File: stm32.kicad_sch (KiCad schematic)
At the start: 12 parts, among them U1 STM32H743VGTx, Y1 32.768MHz, Y2 LFXTAL078719Cutt

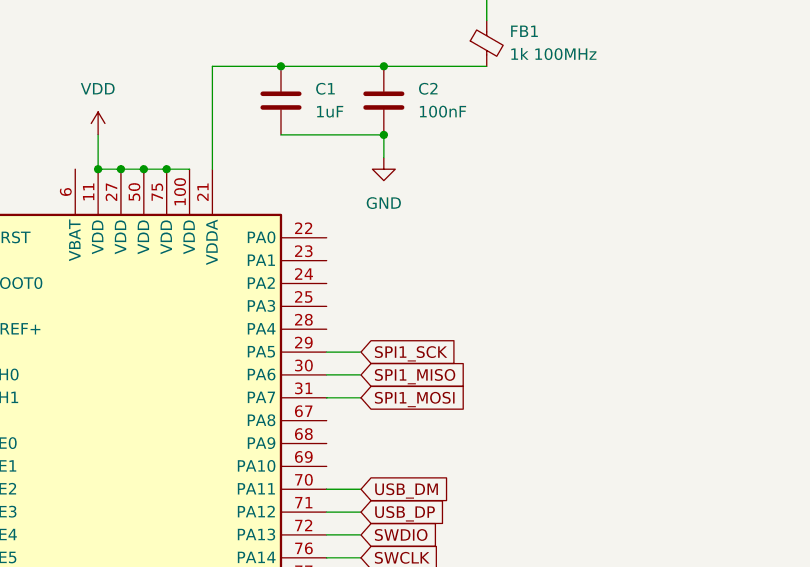
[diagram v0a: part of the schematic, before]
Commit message: Added all sensors and telemetry modem
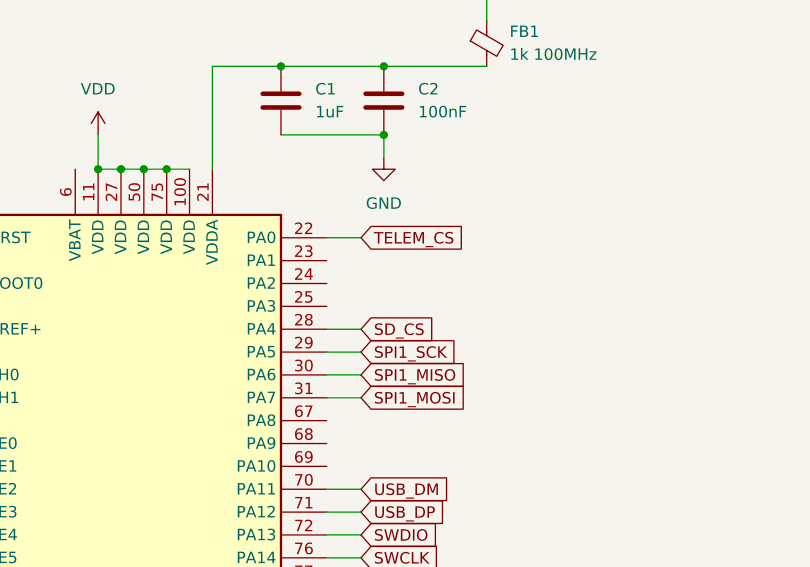
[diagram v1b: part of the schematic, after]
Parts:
- C16, C17, C18, C19: footprint Capacitor_SMD:C_0201_0603Metric -> Capacitor_SMD:C_0402_1005Metric
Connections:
- net TELEM_CS: now reaches U1.22 (PA0)
- net SD_CS: now reaches U1.28 (PA4)
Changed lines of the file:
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@@
+	(wire
+		(pts
+			(xy 152.4 59.69) (xy 156.21 59.69)
+		)
+		(stroke
+			(width 0)
+			(type default)
+		)
+	)
 	(wire
 		(pts
@@
 		(pts
 			(xy 99.06 161.29) (xy 99.06 158.75)
+		)
+		(stroke
+			(width 0)
+			(type default)
+		)
+	)
+	(wire
+		(pts
+			(xy 152.4 49.53) (xy 156.21 49.53)
 		)
 		(stroke
@@
 		(property "Intersheetrefs" "${INTERSHEET_REFS}"
 			(at 166.5128 80.01 0)
+			(effects
+				(font
+					(size 1.27 1.27)
+				)
+				(justify left)
+				(hide yes)
+			)
+		)
+	)
+	(global_label "SD_CS"
+		(shape input)
+		(at 156.21 59.69 0)
+		(fields_autoplaced yes)
+		(effects
+			(font
+				(size 1.27 1.27)
+			)
+			(justify left)
+		)
+		(property "Intersheetrefs" "${INTERSHEET_REFS}"
+			(at 165.1218 59.69 0)
+			(effects
+				(font
+					(size 1.27 1.27)
+				)
+				(justify left)
+				(hide yes)
+			)
+		)
+	)
+	(global_label "TELEM_CS"
+		(shape input)
+		(at 156.21 49.53 0)
+		(fields_autoplaced yes)
+		(effects
+			(font
+				(size 1.27 1.27)
+			)
+			(justify left)
+		)
+		(property "Intersheetrefs" "${INTERSHEET_REFS}"
+			(at 168.3874 49.53 0)
 			(effects
 				(font
@@
 			)
 		)
-		(property "Footprint" "Capacitor_SMD:C_0201_0603Metric"
+		(property "Footprint" "Capacitor_SMD:C_0402_1005Metric"
 			(at 254 59.9948 0)
 			(effects
@@
 			)
 		)
-		(property "Footprint" "Capacitor_SMD:C_0201_0603Metric"
+		(property "Footprint" "Capacitor_SMD:C_0402_1005Metric"
 			(at 269.5448 90.17 0)
 			(effects
@@
 			)
 		)
-		(property "Footprint" "Capacitor_SMD:C_0201_0603Metric"
+		(property "Footprint" "Capacitor_SMD:C_0402_1005Metric"
 			(at 254 42.2148 0)
 			(effects
@@
 			)
 		)
-		(property "Footprint" "Capacitor_SMD:C_0201_0603Metric"
+		(property "Footprint" "Capacitor_SMD:C_0402_1005Metric"
 			(at 212.3948 91.44 0)
 			(effects

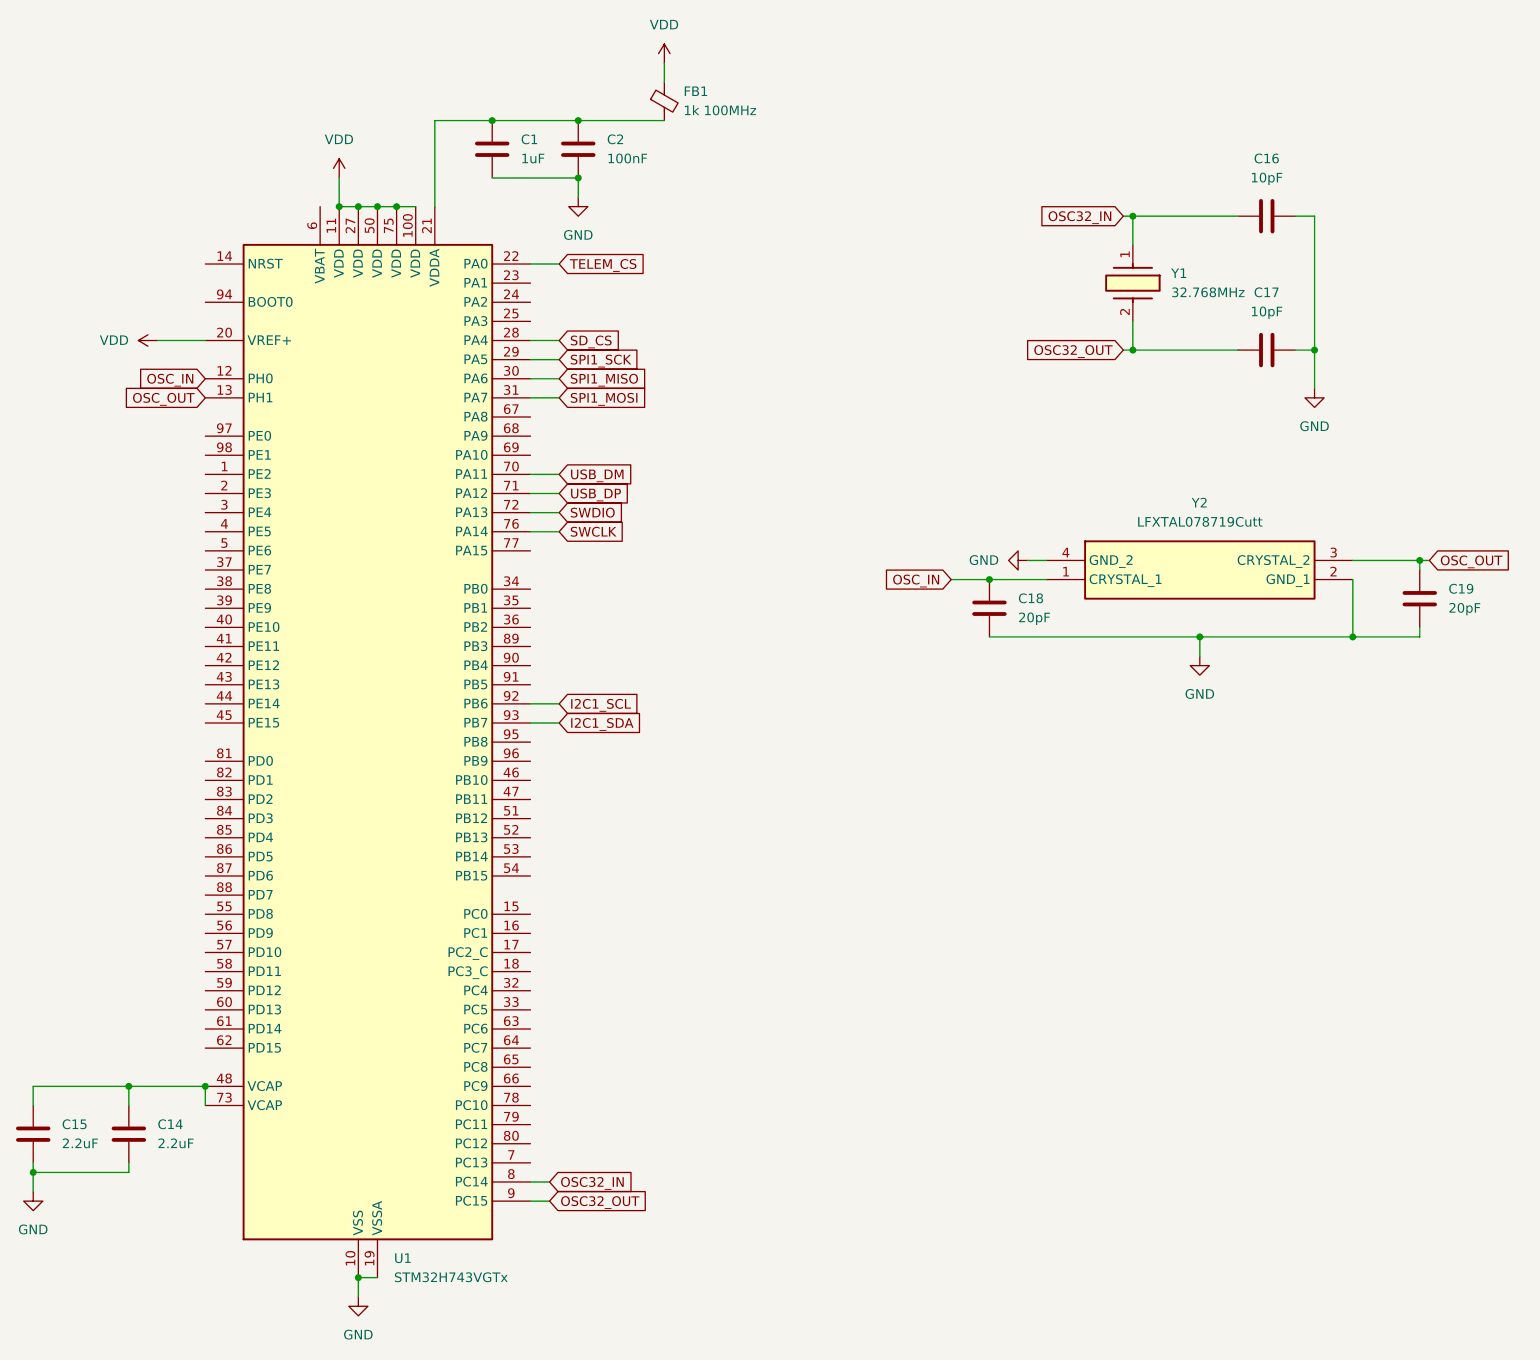
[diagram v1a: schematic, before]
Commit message: Added IO
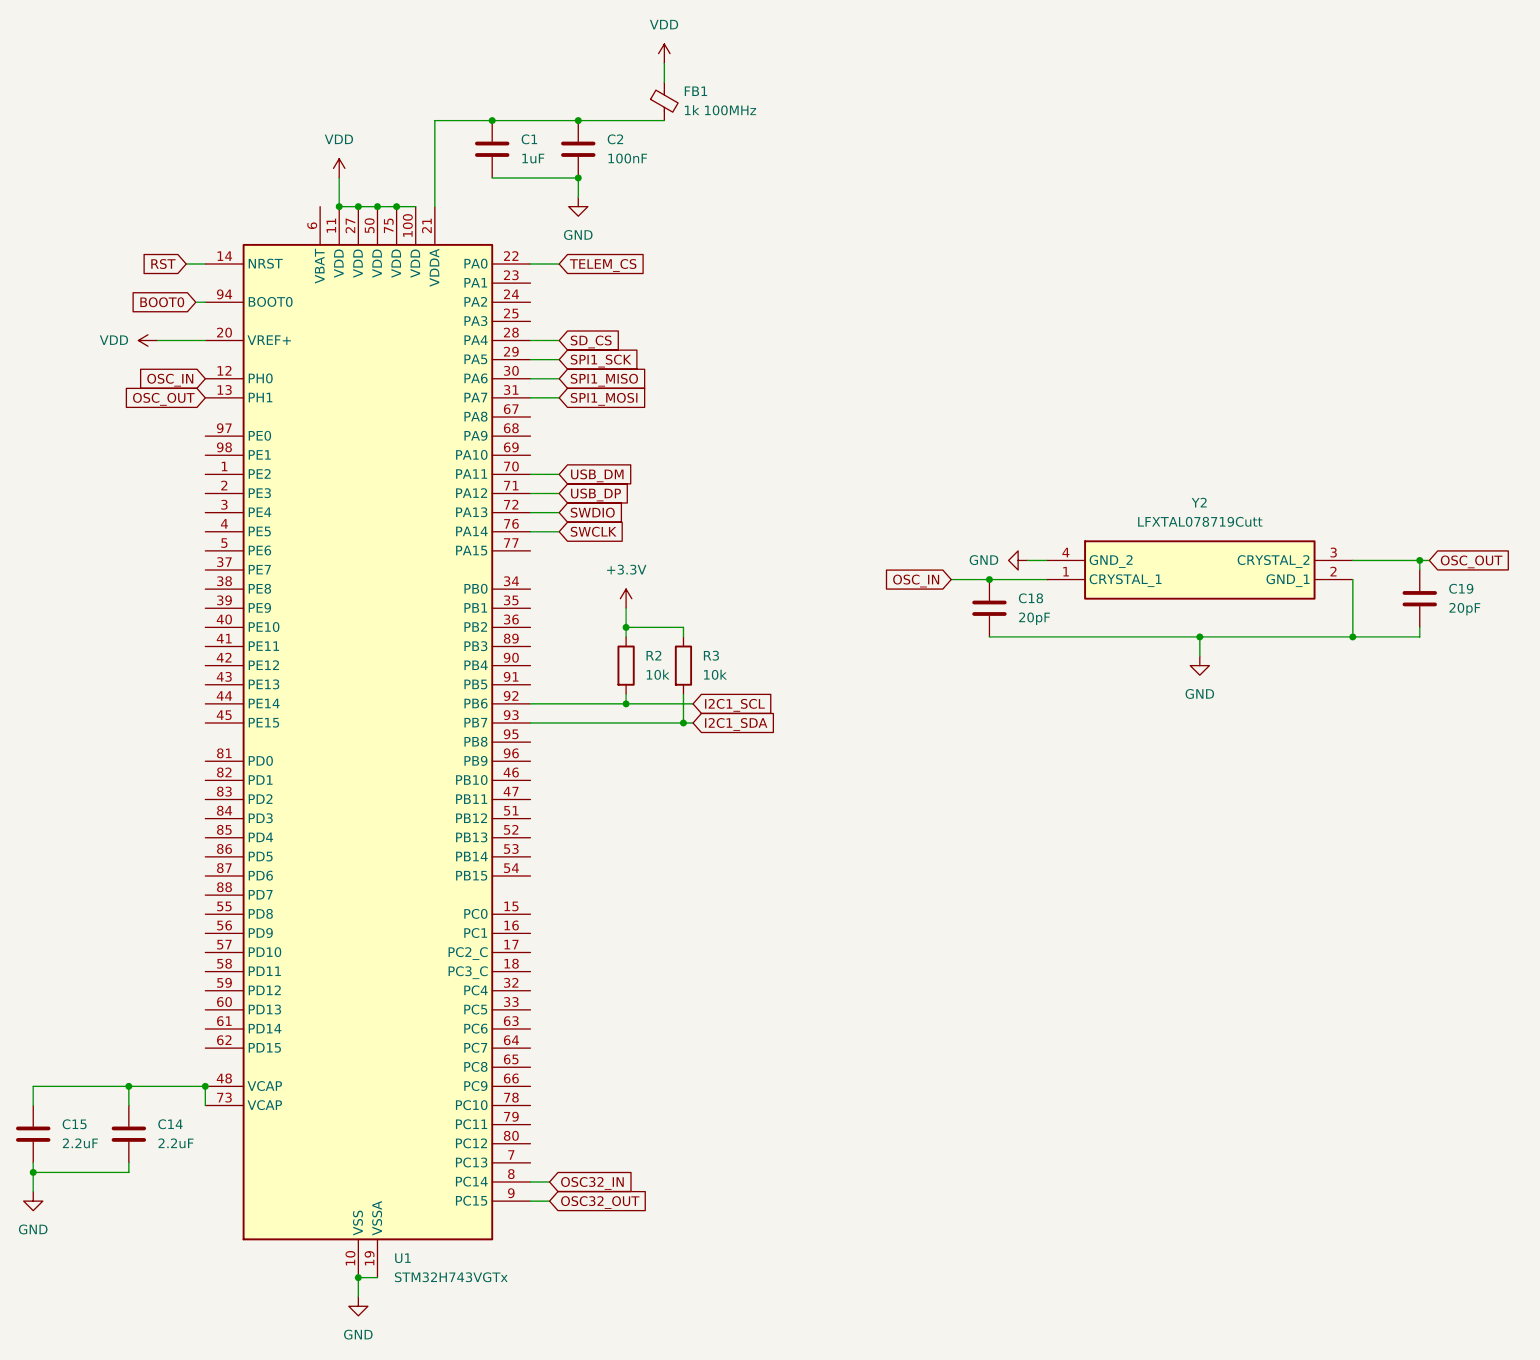
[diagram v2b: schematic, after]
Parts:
- removed C16, C17: 10pF, Capacitor_SMD:C_0402_1005Metric, symbol Device:C
- removed Y1: 32.768MHz, ABM3, symbol VanguardLib:ABM3-32.768MHZ-E4H-T
- added R2, R3: 10k, Resistor_SMD:R_0402_1005Metric, symbol Device:R
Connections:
- net I2C1_SCL: now also R2.2
- net I2C1_SDA: now also R3.2
- net RST: now reaches U1.14 (NRST)
- net BOOT0: now reaches U1.94 (BOOT0)
- new net +3.3V: R2.1, R3.1
